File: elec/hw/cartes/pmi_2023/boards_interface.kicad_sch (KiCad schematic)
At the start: 2 parts

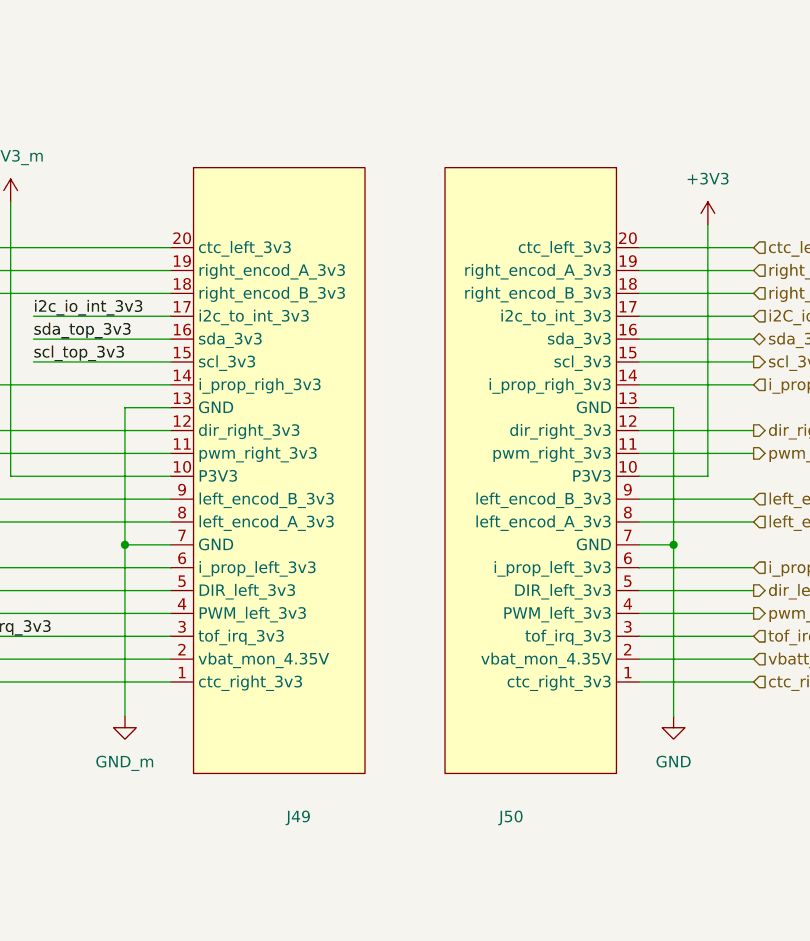
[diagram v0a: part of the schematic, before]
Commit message: PAMI 2023: update jlc part number
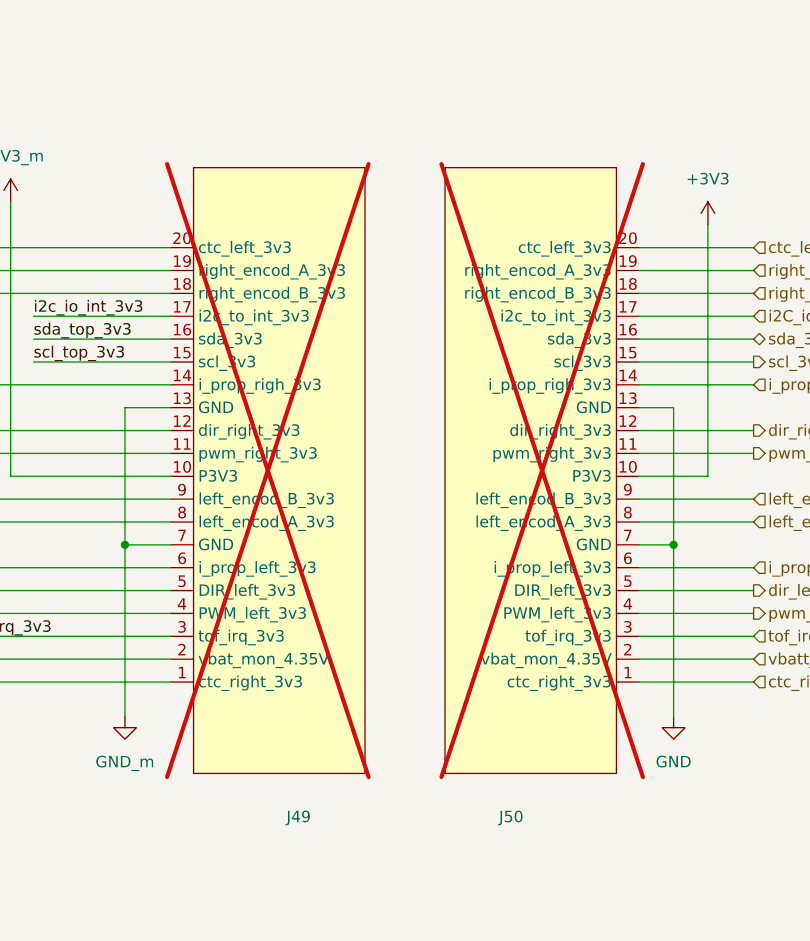
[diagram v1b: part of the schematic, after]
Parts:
- J49, J50: now not fitted
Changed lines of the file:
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@@
 		(in_bom no)
 		(on_board yes)
-		(dnp no)
+		(dnp yes)
 		(property "Reference" "J49"
 			(at 205.994 125.476 0)
@@
 		(in_bom no)
 		(on_board yes)
-		(dnp no)
+		(dnp yes)
 		(property "Reference" "J50"
 			(at 229.616 125.476 0)

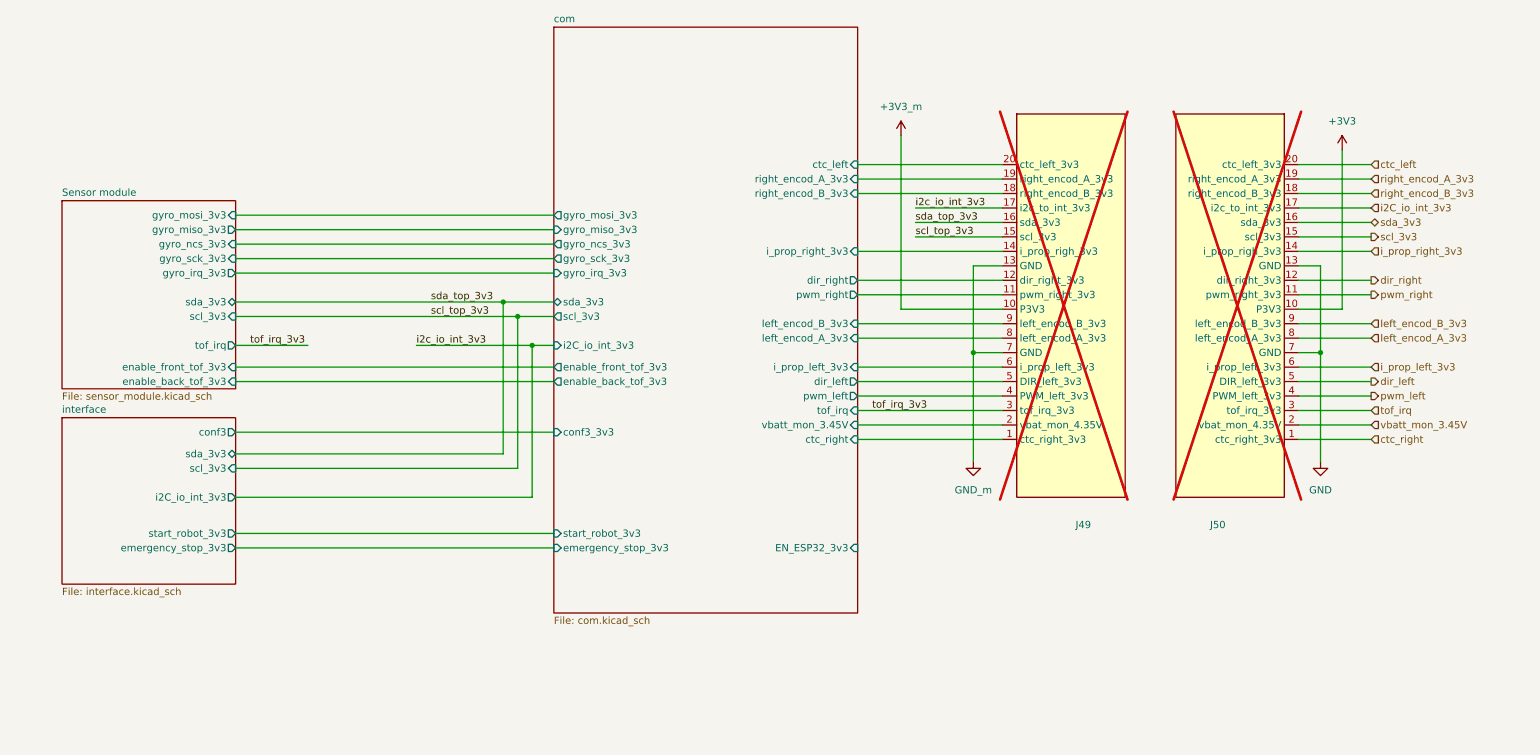
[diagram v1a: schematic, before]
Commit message: pmi_tof_sensor : last commit before tmf8821 deletion
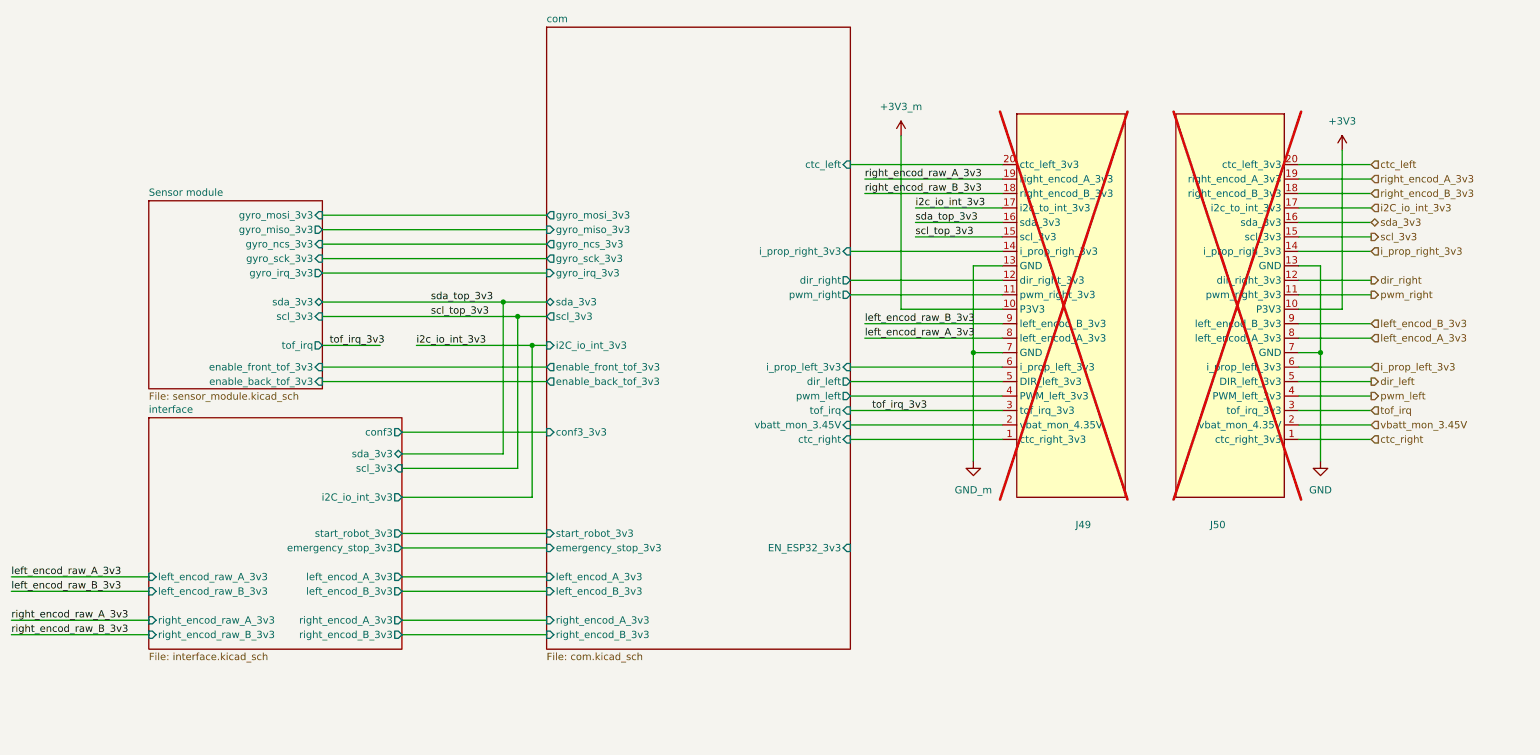
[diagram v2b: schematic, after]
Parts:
- J49: footprint pmi_2023_specific:pmi_2023_interconnection -> pmi_2023_specific:pmi_2023_interconnection_top
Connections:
- net com/left_encod_A_3v3: no longer J49.8 (left_encod_A_3v3)
- net com/left_encod_B_3v3: no longer J49.9 (left_encod_B_3v3)
- net com/right_encod_A_3v3: no longer J49.19 (right_encod_A_3v3)
- net com/right_encod_B_3v3: no longer J49.18 (right_encod_B_3v3)
- new net left_encod_raw_A_3v3: J49.8 (left_encod_A_3v3)
- new net left_encod_raw_B_3v3: J49.9 (left_encod_B_3v3)
- new net right_encod_raw_A_3v3: J49.19 (right_encod_A_3v3)
- new net right_encod_raw_B_3v3: J49.18 (right_encod_B_3v3)
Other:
- sheet interface ports: added left_encod_A_3v3, left_encod_B_3v3, left_encod_raw_A_3v3, left_encod_raw_B_3v3, right_encod_A_3v3, right_encod_B_3v3, right_encod_raw_A_3v3, right_encod_raw_B_3v3; removed none

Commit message: pmi board V2, ready for review
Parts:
- J49: footprint pmi_2023_specific:pmi_2023_interconnection_top -> pmi_2023_specific:pmi_2023_interconnection; symbol pmi_2023_specific:interconnect -> pmi_2023_specific:interconnect_V2; now fitted
- J50: symbol pmi_2023_specific:interconnect -> pmi_2023_specific:interconnect_V2; now fitted
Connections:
- net com/i_prop_left_3v3 is gone; now on net GND_m: J49.6 (GND)
- net i_prop_left_3v3 is gone; now on net GND: J50.6 (GND)
- net +3V3: now also J50.9 (P3V3); no longer J50.10 (P3V3)
- net +3V3_m: now also J49.9 (P3V3); no longer J49.10 (P3V3)
- net GND: now also J50.12 (GND); no longer J50.13 (GND), J50.7 (GND)
- net GND_m: now also J49.12 (GND); no longer J49.13 (GND), J49.7 (GND)
- net com/dir_right: now also J49.11 (dir_right_3v3); no longer J49.12 (dir_right_3v3)
- net com/pwm_right: now also J49.10 (pwm_right_3v3); no longer J49.11 (pwm_right_3v3)
- net dir_right: now also J50.11 (dir_right_3v3); no longer J50.12 (dir_right_3v3)
- net left_encod_A_3v3: now also J50.7 (left_encod_A_3v3); no longer J50.8 (left_encod_A_3v3)
- net left_encod_B_3v3: now also J50.8 (left_encod_B_3v3); no longer J50.9 (left_encod_B_3v3)
- net left_encod_raw_A_3v3: now also J49.7 (left_encod_A_3v3); no longer J49.8 (left_encod_A_3v3)
- net left_encod_raw_B_3v3: now also J49.8 (left_encod_B_3v3); no longer J49.9 (left_encod_B_3v3)
- net pwm_right: now also J50.10 (pwm_right_3v3); no longer J50.11 (pwm_right_3v3)
- net com/i_prop_right_3v3 renamed sda_top_tof_3v3
- net i_prop_right_3v3 renamed sda_tof_3v3
- new net scl_tof_3v3: J50.13 (scl_tof_3v3)
- new net scl_top_tof_3v3: J49.13 (scl_tof_3v3)
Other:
- sheet Sensor module ports: added scl_tof_3v3, sda_tof_3v3; removed scl_3v3, sda_3v3
- sheet com ports: added scl_tof_3v3, sda_tof_3v3; removed i_prop_left_3v3, i_prop_right_3v3

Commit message: pmi board V2, ready for review
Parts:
- J50: footprint pmi_2023_specific:pmi_2023_interconnection -> pmi_2023_specific:pmi_2023_interconnection_bot
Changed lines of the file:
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@@
 			)
 		)
-		(property "Footprint" "pmi_2023_specific:pmi_2023_interconnection"
+		(property "Footprint" "pmi_2023_specific:pmi_2023_interconnection_bot"
 			(at 242.57 93.98 0)
 			(effects

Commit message: pmi : wip
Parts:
- added C22, C54: 100nF 50V, cocotter_capacitors:C_0603_1608Metric, symbol cocotter_capacitors:C_100nF_50V_0603
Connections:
- net GND_m: now also C22.2, C54.2
- net com/ctc_left: now also C22.1
- net com/ctc_right: now also C54.1

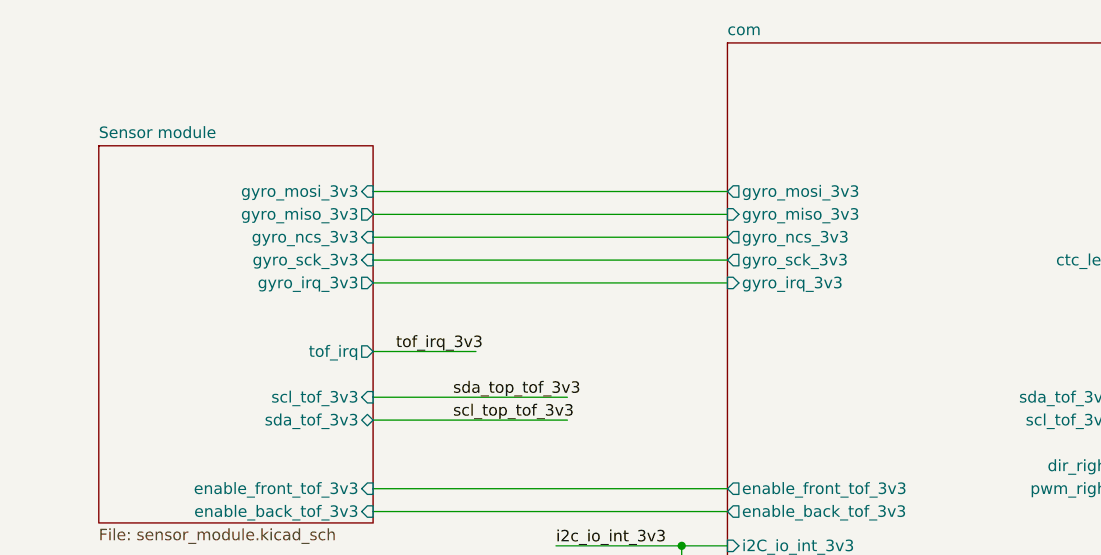
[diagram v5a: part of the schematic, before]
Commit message: pmi : replaced accelerometer and gyroscope with BMI088
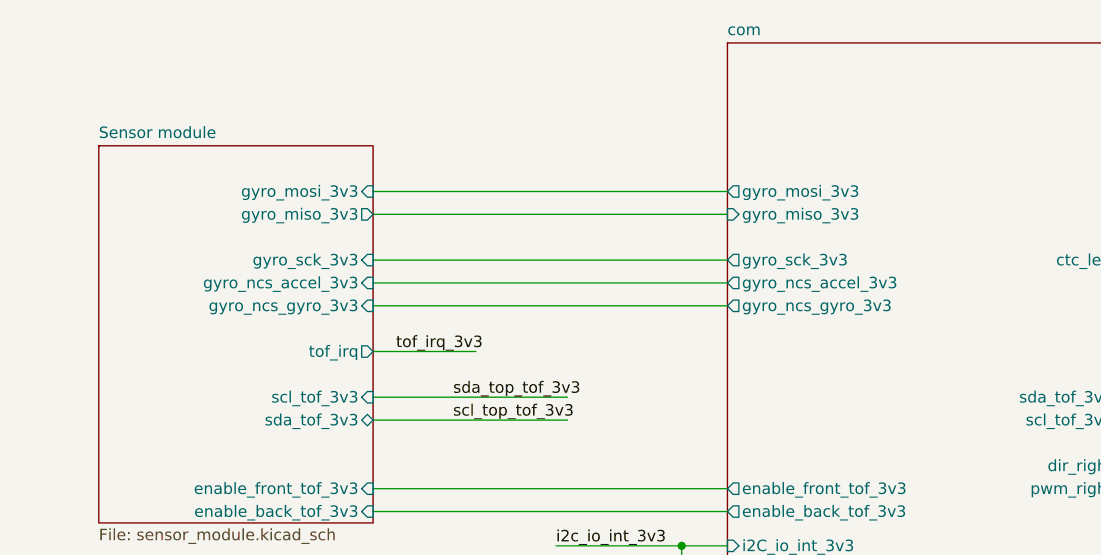
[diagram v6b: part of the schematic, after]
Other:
- sheet Sensor module ports: added gyro_ncs_accel_3v3, gyro_ncs_gyro_3v3; removed gyro_irq_3v3, gyro_ncs_3v3
- sheet com ports: added gyro_ncs_accel_3v3, gyro_ncs_gyro_3v3; removed gyro_irq_3v3, gyro_ncs_3v3
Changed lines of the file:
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@@
 (kicad_sch
-	(version 20231120)
+	(version 20250114)
 	(generator "eeschema")
-	(generator_version "8.0")
+	(generator_version "9.0")
 	(paper "A4")
 	(junction
@@
 	(wire
 		(pts
-			(xy 72.39 59.69) (xy 111.76 59.69)
-		)
-		(stroke
-			(width 0)
-			(type default)
-		)
-	)
-	(wire
-		(pts
 			(xy 86.36 113.03) (xy 111.76 113.03)
 		)
@@
 		(pts
 			(xy 156.21 107.95) (xy 198.12 107.95)
+		)
+		(stroke
+			(width 0)
+			(type default)
+		)
+	)
+	(wire
+		(pts
+			(xy 72.39 67.31) (xy 111.76 67.31)
 		)
 		(stroke
@@
 		(at 111.76 38.1)
 		(size 44.45 109.22)
+		(exclude_from_sim no)
+		(in_bom yes)
+		(on_board yes)
+		(dnp no)
 		(fields_autoplaced yes)
 		(stroke
@@
 			)
 		)
-		(pin "gyro_ncs_3v3" output
-			(at 111.76 59.69 180)
+		(pin "gyro_ncs_gyro_3v3" output
+			(at 111.76 67.31 180)
 			(effects
 				(font
@@
 			)
 		)
-		(pin "gyro_irq_3v3" input
+		(pin "gyro_ncs_accel_3v3" output
 			(at 111.76 64.77 180)
 			(effects
@@
 		(at 41.91 106.68)
 		(size 44.45 40.64)
+		(exclude_from_sim no)
+		(in_bom yes)
+		(on_board yes)
+		(dnp no)
 		(fields_autoplaced yes)
 		(stroke
@@
 		(at 41.91 49.53)
 		(size 30.48 41.91)
+		(exclude_from_sim no)
+		(in_bom yes)
+		(on_board yes)
+		(dnp no)
 		(fields_autoplaced yes)
 		(stroke
@@
 			)
 		)
-		(pin "gyro_ncs_3v3" input
-			(at 72.39 59.69 0)
-			(effects
-				(font
-					(size 1.27 1.27)
-				)
-				(justify right)
-			)
-		)
 		(pin "gyro_sck_3v3" input
 			(at 72.39 62.23 0)
@@
 			)
 		)
-		(pin "gyro_irq_3v3" output
-			(at 72.39 64.77 0)
-			(effects
-				(font
-					(size 1.27 1.27)
-				)
-				(justify right)
-			)
-		)
 		(pin "tof_irq" output
 			(at 72.39 72.39 0)
@@
 			(effects
 				(font
+					(size 1.27 1.27)
+				)
+				(justify right)
+			)
+		)
+		(pin "gyro_ncs_gyro_3v3" input
+			(at 72.39 67.31 0)
+			(effects
+				(font
+					(size 1.27 1.27)
+				)
+				(justify right)
+			)
+		)
+		(pin "gyro_ncs_accel_3v3" input
+			(at 72.39 64.77 0)
+			(effects
+				(font

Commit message: pmi: beginning of transition toward 0402 resistors and capacitors, battery gauge added
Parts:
- C22, C54: footprint cocotter_capacitors:C_0603_1608Metric -> cocotter_capacitors:C_0402_1005Metric; symbol cocotter_capacitors:C_100nF_50V_0603 -> cocotter_capacitors:C_100nF_50V_0402; JLCPCB Part # C14663 -> C85858; Specification 100nF 50V X7R 0603 -> 100nF 50V X7R 0402
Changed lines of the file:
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@@
+			)
+		)
+		(property "JLCPCB" ""
+			(at 204.47 85.09 0)
+			(effects
+				(font
+					(size 1.27 1.27)
+				)
+				(hide yes)
+			)
+		)
+		(property "Sim.Device" ""
+			(at 204.47 85.09 0)
+			(effects
+				(font
+					(size 1.27 1.27)
+				)
+				(hide yes)
+			)
+		)
+		(property "Sim.Pins" ""
+			(at 204.47 85.09 0)
+			(effects
+				(font
+					(size 1.27 1.27)
+				)
+				(hide yes)
+			)
+		)
+		(property "specification" ""
+			(at 204.47 85.09 0)
+			(effects
+				(font
+					(size 1.27 1.27)
+				)
+				(hide yes)
 			)
 		)
@@
 	)
 	(symbol
-		(lib_id "cocotter_capacitors:C_100nF_50V_0603")
+		(lib_id "cocotter_capacitors:C_100nF_50V_0402")
 		(at 160.02 118.11 0)
 		(unit 1)
@@
 			)
 		)
-		(property "Footprint" "cocotter_capacitors:C_0603_1608Metric"
+		(property "Footprint" "cocotter_capacitors:C_0402_1005Metric"
 			(at 160.9852 121.92 0)
 			(effects
@@
 			)
 		)
-		(property "Specification" "100nF 50V X7R 0603 "
-			(at 160.02 118.11 0)
-			(effects
-				(font
-					(size 1.27 1.27)
-				)
-				(hide yes)
-			)
-		)
-		(property "JLCPCB Part #" "C14663"
+		(property "Specification" "100nF 50V X7R 0402"
+			(at 160.02 118.11 0)
+			(effects
+				(font
+					(size 1.27 1.27)
+				)
+				(hide yes)
+			)
+		)
+		(property "JLCPCB Part #" "C85858"
+			(at 160.02 118.11 0)
+			(effects
+				(font
+					(size 1.27 1.27)
+				)
+				(hide yes)
+			)
+		)
+		(property "JLCPCB" ""
+			(at 160.02 118.11 0)
+			(effects
+				(font
+					(size 1.27 1.27)
+				)
+				(hide yes)
+			)
+		)
+		(property "Sim.Device" ""
+			(at 160.02 118.11 0)
+			(effects
+				(font
+					(size 1.27 1.27)
+				)
+				(hide yes)
+			)
+		)
+		(property "Sim.Pins" ""
+			(at 160.02 118.11 0)
+			(effects
+				(font
+					(size 1.27 1.27)
+				)
+				(hide yes)
+			)
+		)
+		(property "specification" ""
 			(at 160.02 118.11 0)
 			(effects
@@
 	)
 	(symbol
-		(lib_id "cocotter_capacitors:C_100nF_50V_0603")
+		(lib_id "cocotter_capacitors:C_100nF_50V_0402")
 		(at 176.53 118.11 0)
 		(unit 1)
@@
 			)
 		)
-		(property "Footprint" "cocotter_capacitors:C_0603_1608Metric"
+		(property "Footprint" "cocotter_capacitors:C_0402_1005Metric"
 			(at 177.4952 121.92 0)
 			(effects
@@
 			)
 		)
-		(property "Specification" "100nF 50V X7R 0603 "
-			(at 176.53 118.11 0)
-			(effects
-				(font
-					(size 1.27 1.27)
-				)
-				(hide yes)
-			)
-		)
-		(property "JLCPCB Part #" "C14663"
+		(property "Specification" "100nF 50V X7R 0402"
+			(at 176.53 118.11 0)
+			(effects
+				(font
+					(size 1.27 1.27)
+				)
+				(hide yes)
+			)
+		)
+		(property "JLCPCB Part #" "C85858"
+			(at 176.53 118.11 0)
+			(effects
+				(font
+					(size 1.27 1.27)
+				)
+				(hide yes)
+			)
+		)
+		(property "JLCPCB" ""
+			(at 176.53 118.11 0)
+			(effects
+				(font
+					(size 1.27 1.27)
+				)
+				(hide yes)
+			)
+		)
+		(property "Sim.Device" ""
+			(at 176.53 118.11 0)
+			(effects
+				(font
+					(size 1.27 1.27)
+				)
+				(hide yes)
+			)
+		)
+		(property "Sim.Pins" ""
+			(at 176.53 118.11 0)
+			(effects
+				(font
+					(size 1.27 1.27)
+				)
+				(hide yes)
+			)
+		)
+		(property "specification" ""
 			(at 176.53 118.11 0)
 			(effects
@@
 			(effects
 				(font
+					(size 1.27 1.27)
+				)
+				(hide yes)
+			)
+		)
+		(property "JLCPCB" ""
+			(at 242.57 85.09 0)
+			(effects
+				(font
+					(size 1.27 1.27)
+				)
+				(hide yes)
+			)
+		)
+		(property "Sim.Device" ""
+			(at 242.57 85.09 0)
+			(effects
+				(font
+					(size 1.27 1.27)
+				)
+				(hide yes)
+			)
+		)
+		(property "Sim.Pins" ""
+			(at 242.57 85.09 0)
+			(effects
+				(font
+					(size 1.27 1.27)
+				)
+				(hide yes)
+			)
+		)
+		(property "specification" ""
+			(at 242.57 85.09 0)
+			(effects
+				(font
